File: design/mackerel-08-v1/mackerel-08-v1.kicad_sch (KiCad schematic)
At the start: 38 parts, among them J2 DC_Jack, J3 Conn_01x06, J4 Conn_01x06, J5 Conn_02x20_Odd_Even, SW1 SW_Push, U1 MC68008, U10 74HC595, U11 74HC10, U12 GAL16V8, U13 GAL16V8, U14 NE555P, U2 AS7C4096A, U3 AS7C4096A, U4 AS7C4096A, U5 AS7C4096A, U6 AS7C4096A, U7 AS7C4096A, U8 SST39SF040, U9 XR68C681, X1 CXO_DIP8, X2 CXO_DIP8

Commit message: Full interrupt and IACK decoding in PLD
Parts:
- removed J5: Conn_02x20_Odd_Even, Connector_PinHeader_2.54mm:PinHeader_2x20_P2.54mm_Vertical, symbol Connector_Generic:Conn_02x20_Odd_Even
- removed U12, U13: GAL16V8, Package_DIP:DIP-20_W7.62mm_Socket_LongPads, symbol Logic_Programmable:GAL16V8
- added U12, U?: ATF22V10C, Package_DIP:DIP-24_W7.62mm_Socket_LongPads, symbol mackerel-68k-symbols:ATF22V10C
- added U?: AS7C4096A, Package_SO:SOJ-36_10.16x23.49mm_P1.27mm, symbol mackerel-68k-symbols:AS7C4096A
- U14: footprint Package_DIP:DIP-8_W7.62mm -> Package_DIP:DIP-8_W7.62mm_Socket_LongPads
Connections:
- net +5V: now also U12.24 (vcc), U?.24 (vcc), U?.27 (VCC), U?.9 (VCC)
- net A0: now also U?.1 (A0)
- net A1: now also U12.4 (IN3/PD), U?.2 (A1), U?.9 (IN8)
- net A10: now also U?.20 (A10)
- net A11: now also U?.21 (A11)
- net A12: now also U?.22 (A12)
- net A13: now also U?.23 (A13)
- net A14: now also U?.24 (A14)
- net A15: now also U?.32 (A15)
- net A16: now also U12.7 (IN6), U?.33 (A16)
- net A17: now also U12.8 (IN7), U?.34 (A17)
- net A18: now also U12.9 (IN8), U?.35 (A18)
- net A19: now also U12.10 (IN9)
- net A2: now also U12.5 (IN4), U?.10 (IN9), U?.3 (A2)
- net A20: now also U12.11 (IN10)
- net A21: now also U12.13 (IN11)
- net A3: now also U12.6 (IN5), U?.11 (IN10), U?.4 (A3)
- net A4: now also U?.5 (A4)
- net A5: now also U?.14 (A5)
- net A6: now also U?.15 (A6)
- net A7: now also U?.16 (A7)
- net A8: now also U?.17 (A8)
- net A9: now also U?.18 (A9)
- net BOOT: now also U12.1 (CLK/IN0)
- net D0: now also U?.7 (IO1)
- net D1: now also U?.8 (IO2)
- net D2: now also U?.11 (IO3)
- net D3: now also U?.12 (IO4)
- net D4: now also U?.25 (IO5)
- net D5: now also U?.26 (IO6)
- net D6: now also U?.29 (IO7)
- net D7: now also U?.30 (IO8)
- net GND: now also U12.12 (GND), U?.10 (GND), U?.12 (GND), U?.28 (GND), U?.31 (OE)
- net RAM_EN0: now also U12.19 (IO5)
- net RAM_EN1: now also U12.18 (IO4)
- net RAM_EN2: now also U12.17 (IO3)
- net RAM_EN3: now also U12.16 (IO2)
- net RAM_EN4: now also U12.15 (IO1)
- net RAM_EN5: now also U12.14 (IO0)
- net /AS: now also U12.2 (IN1), U?.13 (IN11)
- net /CS_DUART: now also U12.22 (IO8); no longer U9.39 (CS)
- net /CS_ROM: now also U12.20 (IO6)
- net /IACK: now also U12.3 (IN2), U?.8 (IN7)
- net /IACK_DUART: now also U12.23 (IO9); no longer R2.1, U9.41 (/IACK)
- net /IPL0: now also U?.21 (IO7)
- net /IPL1: now also U?.22 (IO8)
- net /IPL2: now also U?.23 (IO9)
- net /RW: now also U?.13 (WE)
- net /IRQ_DUART renamed /IRQ1
- net /IRQ1: now also U?.1 (CLK/IN0)
- new net RAM_EN6: U?.6 (CE)
- new net /CS0: U9.39 (CS)
- new net /CS_IO: U12.21 (IO7)
- new net /IACK1: R2.1, U9.41 (/IACK), U?.14 (IO0)
- new net /IACK2: U?.15 (IO1)
- new net /IACK3: U?.16 (IO2)
- new net /IACK4: U?.17 (IO3)
- new net /IACK5: U?.18 (IO4)
- new net /IACK6: U?.19 (IO5)
- new net /IACK7: U?.20 (IO6)
- new net /IRQ2: U?.2 (IN1)
- new net /IRQ3: U?.3 (IN2)
- new net /IRQ4: U?.4 (IN3/PD)
- new net /IRQ5: U?.5 (IN4)
- new net /IRQ6: U?.6 (IN5)
- new net /IRQ7: U?.7 (IN6)
- no-connect marks 76 -> 38
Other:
- note added: "Interrupt/IACK Decoder"
- note removed: "Address/Interrupt Decoder"
- note removed: "RAM Chip Selector"
- note removed: "TODO: redo this bus layout"
- moved on the sheet: C1, D1, D2, R10, R11, R12, R13, SW1, U14, U6, U7

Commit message: Mackerel-08 mostly routed
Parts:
- removed J3, J4: Conn_01x06, Connector_PinHeader_2.54mm:PinHeader_1x06_P2.54mm_Vertical, symbol Connector_Generic:Conn_01x06
- removed R1: R, Resistor_SMD:R_1206_3216Metric_Pad1.30x1.75mm_HandSolder, symbol Device:R
- removed U11: 74HC10, Package_DIP:DIP-14_W7.62mm_Socket_LongPads, symbol mackerel-68k-symbols:74HC10
- removed U?: AS7C4096A, Package_SO:SOJ-36_10.16x23.49mm_P1.27mm, symbol mackerel-68k-symbols:AS7C4096A
- added J1: Conn_02x20_Odd_Even, Connector_PinSocket_2.54mm:PinSocket_2x20_P2.54mm_Horizontal, symbol Connector_Generic:Conn_02x20_Odd_Even
- added J3, J4: Conn_02x10_Odd_Even, Connector_PinSocket_2.54mm:PinSocket_2x10_P2.54mm_Horizontal, symbol Connector_Generic:Conn_02x10_Odd_Even
- added J5, J6: Conn_01x06, Connector_PinSocket_2.54mm:PinSocket_1x06_P2.54mm_Horizontal, symbol Connector_Generic:Conn_01x06
- added U13: 74HC10, Package_DIP:DIP-14_W7.62mm_Socket_LongPads, symbol mackerel-68k-symbols:74HC10
- added U8: AS7C4096A, Package_SO:SOJ-36_10.16x23.49mm_P1.27mm, symbol mackerel-68k-symbols:AS7C4096A
- U9: renamed from U8; footprint Package_DIP:DIP-32_W15.24mm_Socket_LongPads -> Socket:DIP_Socket-32_W11.9_W12.7_W15.24_W17.78_W18.5_3M_232-1285-00-0602J
- gave numbers to parts that had none: 1
- renumbered U9 to U10, U10 to U11, U14 to U15
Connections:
- net /CS0 is gone; now on net /DUART0: U10.39 (CS)
- net /CS_DUART is gone; now on net /RAM1: U12.22 (IO8)
- net /IACK_DUART is gone; now on net /RAM0: U12.23 (IO9)
- net +5V: now also J1.1 (Pin_1), J1.2 (Pin_2), J3.1 (Pin_1), J3.2 (Pin_2), J4.1 (Pin_1), J4.2 (Pin_2), U13.14 (VCC), U8.27 (VCC), U8.9 (VCC)
- net A0: now also J1.13 (Pin_13), U8.1 (A0)
- net A1: now also J1.14 (Pin_14), U8.2 (A1); no longer U12.4 (IN3/PD)
- net A10: now also J1.25 (Pin_25), U8.20 (A10)
- net A11: now also J1.26 (Pin_26), U8.21 (A11)
- net A12: now also J1.27 (Pin_27), U8.22 (A12)
- net A13: now also J1.28 (Pin_28), U8.23 (A13)
- net A14: now also J1.29 (Pin_29), U8.24 (A14)
- net A15: now also J1.30 (Pin_30), U8.32 (A15)
- net A16: now also J3.3 (Pin_3), U8.33 (A16)
- net A17: now also J3.4 (Pin_4), U8.34 (A17)
- net A18: now also J3.5 (Pin_5), U8.35 (A18)
- net A19: now also J3.6 (Pin_6)
- net A2: now also J1.15 (Pin_15), U8.3 (A2); no longer U12.5 (IN4)
- net A20: now also J3.7 (Pin_7)
- net A21: now also J3.8 (Pin_8)
- net A3: now also J1.16 (Pin_16), U8.4 (A3); no longer U12.6 (IN5)
- net A4: now also J1.17 (Pin_17), U8.5 (A4)
- net A5: now also J1.18 (Pin_18), U8.14 (A5)
- net A6: now also J1.19 (Pin_19), U8.15 (A6)
- net A7: now also J1.20 (Pin_20), U8.16 (A7)
- net A8: now also J1.23 (Pin_23), U8.17 (A8)
- net A9: now also J1.24 (Pin_24), U8.18 (A9)
- net D0: now also J1.5 (Pin_5), U8.7 (IO1)
- net D1: now also J1.6 (Pin_6), U8.8 (IO2)
- net D2: now also J1.7 (Pin_7), U8.11 (IO3)
- net D3: now also J1.8 (Pin_8), U8.12 (IO4)
- net D4: now also J1.9 (Pin_9), U8.25 (IO5)
- net D5: now also J1.10 (Pin_10), U8.26 (IO6)
- net D6: now also J1.11 (Pin_11), U8.29 (IO7)
- net D7: now also J1.12 (Pin_12), U8.30 (IO8)
- net GND: now also J1.21 (Pin_21), J1.22 (Pin_22), J1.3 (Pin_3), J1.39 (Pin_39), J1.4 (Pin_4), J1.40 (Pin_40), J3.19 (Pin_19), J3.20 (Pin_20), J4.18 (Pin_18), J4.20 (Pin_20), J4.3 (Pin_3), J4.4 (Pin_4), J5.6 (Pin_6), J6.6 (Pin_6), U13.1 (1A), U13.10 (3B), U13.11 (3C), U13.13 (1C), U13.2 (1B), U13.7 (GND), U13.9 (3A), U8.10 (GND), U8.28 (GND), U8.31 (OE)
- net /AS: now also J1.31 (Pin_31)
- net /CS_IO: now also U12.14 (IO0), J1.35 (Pin_35); no longer U12.21 (IO7)
- net /DS: now also J1.32 (Pin_32)
- net /DTACK: now also J1.33 (Pin_33)
- net /IACK: now also J1.34 (Pin_34), U13.6 (2Y)
- net /IACK2: now also J1.38 (Pin_38)
- net /IACK3: now also J3.10 (Pin_10)
- net /IACK4: now also J3.12 (Pin_12)
- net /IACK5: now also J3.14 (Pin_14)
- net /IACK6: now also J3.16 (Pin_16)
- net /IACK7: now also J3.18 (Pin_18)
- net /IRQ2: now also J1.37 (Pin_37)
- net /IRQ3: now also J3.9 (Pin_9)
- net /IRQ4: now also J3.11 (Pin_11)
- net /IRQ5: now also J3.13 (Pin_13)
- net /IRQ6: now also J3.15 (Pin_15)
- net /IRQ7: now also J3.17 (Pin_17)
- net /RESET: now also J1.36 (Pin_36)
- net /RW: now also U8.13 (WE)
- net at R7.1: now also U1.36 (/BGACK); no longer U1.37 (/BR)
- net OP1: now reaches U10.14 (OP1)
- net OP1: now also J4.7 (Pin_7)
- net OP3: now reaches U10.15 (OP3)
- net OP3: now also J4.11 (Pin_11)
- net OP5: now reaches U10.16 (OP5)
- net OP5: now also J4.15 (Pin_15)
- net OP7: now reaches U10.17 (OP7)
- net OP7: now also J4.19 (Pin_19)
- net OP6: now reaches U10.29 (OP6)
- net OP6: now also J4.17 (Pin_17)
- net IP3: now reaches U10.3 (IP3)
- net IP3: now also J4.12 (Pin_12)
- net OP4: now reaches U10.30 (OP4)
- net OP4: now also J4.13 (Pin_13)
- net OP2: now reaches U10.31 (OP2)
- net OP2: now also J4.9 (Pin_9)
- net OP0: now reaches U10.32 (OP0)
- net OP0: now also J4.5 (Pin_5)
- net IP2: now reaches U10.40 (IP2)
- net IP2: now also J4.10 (Pin_10)
- net IP5: now reaches U10.42 (IP5)
- net IP5: now also J4.16 (Pin_16)
- net IP4: now reaches U10.43 (IP4)
- net IP4: now also J4.14 (Pin_14)
- net IP1: now reaches U10.5 (IP1)
- net IP1: now also J4.8 (Pin_8)
- net IP0: now reaches U10.8 (IP0)
- net IP0: now also J4.6 (Pin_6)
- net at R6.1: now also U1.37 (/BR); no longer U1.43 (/VPA)
- net at R8.1: now also U1.44 (/BERR); no longer U1.36 (/BGACK)
- net CLK_CPU: now reaches U1.38 (CLK), X1.5 (OUT)
- net at R9.1: now also U1.43 (/VPA); no longer U1.44 (/BERR)
- net FC0: no longer names the net of U1.50 (FC0)
- net FC0: now also U13.5 (2C)
- net FC1: no longer names the net of U1.49 (FC1)
- net FC1: now also U13.4 (2B)
- net FC2: no longer names the net of U1.48 (FC2)
- net FC2: now also U13.3 (2A)
- net RAM_EN0 renamed /RAM0
- net /RAM0: no longer U12.19 (IO5)
- net RAM_EN1 renamed /RAM1
- net /RAM1: no longer U12.18 (IO4)
- net RAM_EN2 renamed /RAM2
- net /RAM2: now also U12.21 (IO7); no longer U12.17 (IO3)
- net RAM_EN3 renamed /RAM3
- net /RAM3: now also U12.20 (IO6); no longer U12.16 (IO2)
- net RAM_EN4 renamed /DUART0
- net /DUART0: no longer U6.6 (CE)
- net RAM_EN5 renamed /RAM5
- net /RAM5: now also U12.18 (IO4); no longer U12.14 (IO0)
- net RXA: no longer names the net of U10.35 (RXDA)
- net RXA: now also J5.3 (Pin_3)
- net RXB: no longer names the net of U10.11 (RXDB)
- net RXB: now also J6.3 (Pin_3)
- net TXA: no longer names the net of U10.33 (TXDA)
- net TXA: now also J5.2 (Pin_2)
- net TXB: no longer names the net of U10.13 (TXDB)
- net TXB: now also J6.2 (Pin_2)
- net /CS_ROM renamed /ROM0
- net /ROM0: now also U12.16 (IO2); no longer U12.20 (IO6)
- new net /RAM4: U12.19 (IO5), U6.6 (CE)
- new net /RAM6: U12.17 (IO3), U8.6 (CE)
- no-connect marks 38 -> 27
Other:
- note added: "TODO: Am I using autovector or normal vector?"
- note added: "TODO: Does DTACK factor into IACK signals?"
- note removed: "TODO: expose GPIO pins"
- moved on the sheet: C1, C2, D1, D2, J2, R10, R11, R12, R13, R2, R3, R4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

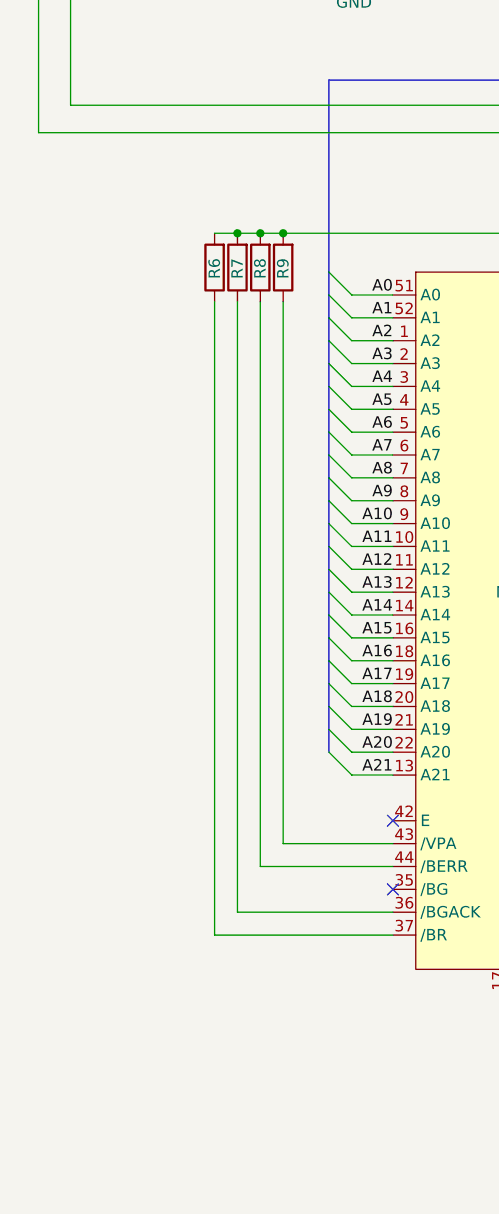
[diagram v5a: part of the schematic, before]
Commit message: Add decoupling caps
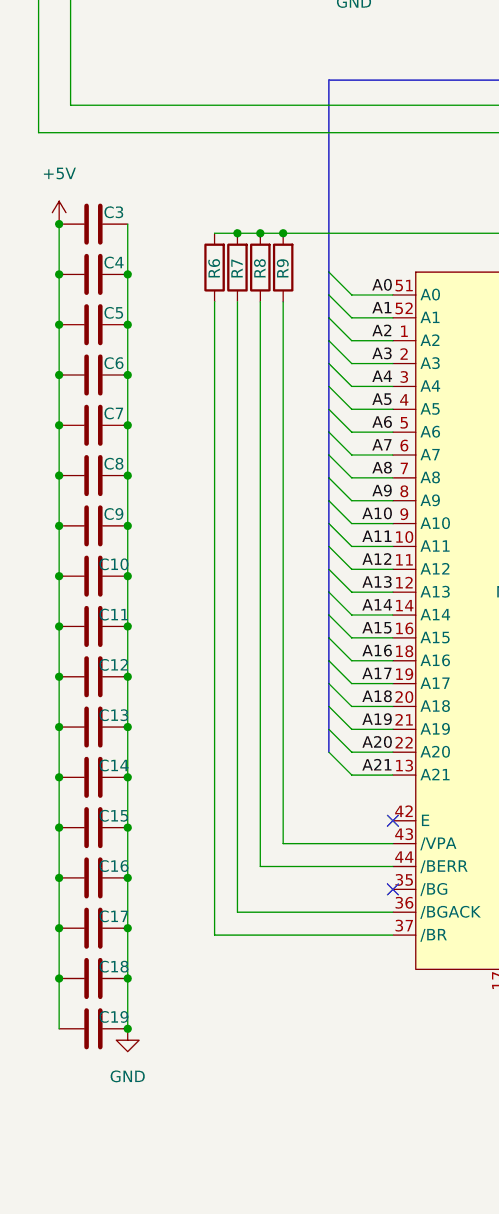
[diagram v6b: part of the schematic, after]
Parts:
- added C10, C11, C12, C13, C14, C15, C16, C17, C18, C19, C3, C4, C5, C6, C7, C8, C9: C, Capacitor_THT:C_Disc_D3.0mm_W2.0mm_P2.50mm, symbol Device:C
- R10, R11, R12, R13, R2, R3, R4, R5, R6, R7, R8, R9: footprint Resistor_SMD:R_1206_3216Metric_Pad1.30x1.75mm_HandSolder -> Resistor_THT:R_Axial_DIN0207_L6.3mm_D2.5mm_P7.62mm_Horizontal
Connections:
- net +5V: now also C10.1, C11.1, C12.1, C13.1, C14.1, C15.1, C16.1, C17.1, C18.1, C19.1, C3.1, C4.1, C5.1, C6.1, C7.1, C8.1, C9.1
- net GND: now also C10.2, C11.2, C12.2, C13.2, C14.2, C15.2, C16.2, C17.2, C18.2, C19.2, C3.2, C4.2, C5.2, C6.2, C7.2, C8.2, C9.2

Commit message: Rough layout of Mackerel-08 Rev1 PCB
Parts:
- removed J1: Conn_02x20_Odd_Even, Connector_PinSocket_2.54mm:PinSocket_2x20_P2.54mm_Horizontal, symbol Connector_Generic:Conn_02x20_Odd_Even
- removed J3, J4: Conn_02x10_Odd_Even, Connector_PinSocket_2.54mm:PinSocket_2x10_P2.54mm_Horizontal, symbol Connector_Generic:Conn_02x10_Odd_Even
- removed J5, J6: Conn_01x06, Connector_PinSocket_2.54mm:PinSocket_1x06_P2.54mm_Horizontal, symbol Connector_Generic:Conn_01x06
- removed U13: 74HC10, Package_DIP:DIP-14_W7.62mm_Socket_LongPads, symbol mackerel-68k-symbols:74HC10
- removed U2, U3, U4, U5, U6, U7, U8: AS7C4096A, Package_SO:SOJ-36_10.16x23.49mm_P1.27mm, symbol mackerel-68k-symbols:AS7C4096A
- added C20, C21, C22, C23, C24, C25, C26, C27: C_Polarized_US, Capacitor_THT:CP_Radial_Tantal_D4.5mm_P5.00mm, symbol Device:C_Polarized_US
- added D3: LED, LED_THT:LED_D5.0mm, symbol Device:LED
- added H1, H2, H3, H4: MountingHole, MountingHole:MountingHole_3.7mm_Pad_Via, symbol Mechanical:MountingHole
- added J1: Conn_01x08, Connector_PinSocket_2.54mm:PinSocket_1x08_P2.54mm_Vertical, symbol Connector_Generic:Conn_01x08
- added J3: Conn_02x20_Counter_Clockwise, symbol Connector_Generic:Conn_02x20_Counter_Clockwise
- added J4: Conn_02x20_Counter_Clockwise, Connector_IDC:IDC-Header_2x20_P2.54mm_Vertical, symbol Connector_Generic:Conn_02x20_Counter_Clockwise
- added J5, J6: DB9_Male_MountingHoles, Connector_Dsub:DSUB-9_Male_Horizontal_P2.77x2.84mm_EdgePinOffset7.70mm_Housed_MountingHolesOffset9.12mm, symbol Connector:DB9_Male_MountingHoles
- added R1, R14, R15: R, Resistor_THT:R_Axial_DIN0207_L6.3mm_D2.5mm_P7.62mm_Horizontal, symbol Device:R
- added SW2: SW_SPDT, herring:SW_Mini_Toggle, symbol Switch:SW_SPDT
- added U13, U16: MAX3232, Package_DIP:DIP-16_W7.62mm, symbol Interface_UART:MAX3232
- added U2, U3, U4, U5, U6, U7, U8: AS6C4008-55PCN, Package_DIP:DIP-32_W15.24mm, symbol Memory_RAM:AS6C4008-55PCN
- U11: footprint Package_DIP:DIP-16_W7.62mm_Socket_LongPads -> Package_DIP:DIP-16_W7.62mm
- U12, U14: footprint Package_DIP:DIP-24_W7.62mm_Socket_LongPads -> Package_DIP:DIP-24_W7.62mm
- U15: footprint Package_DIP:DIP-8_W7.62mm_Socket_LongPads -> Package_DIP:DIP-8_W7.62mm
- U9: footprint Socket:DIP_Socket-32_W11.9_W12.7_W15.24_W17.78_W18.5_3M_232-1285-00-0602J -> Package_DIP:DIP-32_W15.24mm
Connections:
- net /IACK6 is gone; now on net /IACK: U14.19 (IO5)
- net /IRQ4 is gone; now on net FC0: U14.4 (IN3/PD)
- net /IRQ5 is gone; now on net FC1: U14.5 (IN4)
- net /IRQ6 is gone; now on net FC2: U14.6 (IN5)
- net +5V: now also J1.1 (Pin_1), R14.2, R15.2, U13.16 (VCC), U16.16 (VCC), U2.32 (VCC), U3.32 (VCC), U4.32 (VCC), U5.32 (VCC), U6.32 (VCC), U7.32 (VCC), U8.32 (VCC)
- net A0: now also U2.12 (A0), U3.12 (A0), U4.12 (A0), U5.12 (A0), U6.12 (A0), U7.12 (A0), U8.12 (A0)
- net A1: now also U2.11 (A1), U3.11 (A1), U4.11 (A1), U5.11 (A1), U6.11 (A1), U7.11 (A1), U8.11 (A1)
- net A10: now also U2.23 (A10), U3.23 (A10), U4.23 (A10), U5.23 (A10), U6.23 (A10), U7.23 (A10), U8.23 (A10)
- net A11: now also U2.25 (A11), U3.25 (A11), U4.25 (A11), U5.25 (A11), U6.25 (A11), U7.25 (A11), U8.25 (A11)
- net A12: now also U2.4 (A12), U3.4 (A12), U4.4 (A12), U5.4 (A12), U6.4 (A12), U7.4 (A12), U8.4 (A12)
- net A13: now also U2.28 (A13), U3.28 (A13), U4.28 (A13), U5.28 (A13), U6.28 (A13), U7.28 (A13), U8.28 (A13)
- net A14: now also U2.3 (A14), U3.3 (A14), U4.3 (A14), U5.3 (A14), U6.3 (A14), U7.3 (A14), U8.3 (A14)
- net A15: now also U2.31 (A15), U3.31 (A15), U4.31 (A15), U5.31 (A15), U6.31 (A15), U7.31 (A15), U8.31 (A15)
- net A16: now also U2.2 (A16), U3.2 (A16), U4.2 (A16), U5.2 (A16), U6.2 (A16), U7.2 (A16), U8.2 (A16)
- net A17: now also U2.30 (A17), U3.30 (A17), U4.30 (A17), U5.30 (A17), U6.30 (A17), U7.30 (A17), U8.30 (A17)
- net A18: now also U2.1 (A18), U3.1 (A18), U4.1 (A18), U5.1 (A18), U6.1 (A18), U7.1 (A18), U8.1 (A18)
- net A2: now also U2.10 (A2), U3.10 (A2), U4.10 (A2), U5.10 (A2), U6.10 (A2), U7.10 (A2), U8.10 (A2)
- net A3: now also U2.9 (A3), U3.9 (A3), U4.9 (A3), U5.9 (A3), U6.9 (A3), U7.9 (A3), U8.9 (A3)
- net A4: now also U2.8 (A4), U3.8 (A4), U4.8 (A4), U5.8 (A4), U6.8 (A4), U7.8 (A4), U8.8 (A4)
- net A5: now also U2.7 (A5), U3.7 (A5), U4.7 (A5), U5.7 (A5), U6.7 (A5), U7.7 (A5), U8.7 (A5)
- net A6: now also U2.6 (A6), U3.6 (A6), U4.6 (A6), U5.6 (A6), U6.6 (A6), U7.6 (A6), U8.6 (A6)
- net A7: now also U2.5 (A7), U3.5 (A7), U4.5 (A7), U5.5 (A7), U6.5 (A7), U7.5 (A7), U8.5 (A7)
- net A8: now also U2.27 (A8), U3.27 (A8), U4.27 (A8), U5.27 (A8), U6.27 (A8), U7.27 (A8), U8.27 (A8)
- net A9: now also U2.26 (A9), U3.26 (A9), U4.26 (A9), U5.26 (A9), U6.26 (A9), U7.26 (A9), U8.26 (A9)
- net D0: now also U2.13 (DQ0), U3.13 (DQ0), U4.13 (DQ0), U5.13 (DQ0), U6.13 (DQ0), U7.13 (DQ0), U8.13 (DQ0)
- net D1: now also U2.14 (DQ1), U3.14 (DQ1), U4.14 (DQ1), U5.14 (DQ1), U6.14 (DQ1), U7.14 (DQ1), U8.14 (DQ1)
- net D2: now also U2.15 (DQ2), U3.15 (DQ2), U4.15 (DQ2), U5.15 (DQ2), U6.15 (DQ2), U7.15 (DQ2), U8.15 (DQ2)
- net D3: now also U2.17 (DQ3), U3.17 (DQ3), U4.17 (DQ3), U5.17 (DQ3), U6.17 (DQ3), U7.17 (DQ3), U8.17 (DQ3)
- net D4: now also U2.18 (DQ4), U3.18 (DQ4), U4.18 (DQ4), U5.18 (DQ4), U6.18 (DQ4), U7.18 (DQ4), U8.18 (DQ4)
- net D5: now also U2.19 (DQ5), U3.19 (DQ5), U4.19 (DQ5), U5.19 (DQ5), U6.19 (DQ5), U7.19 (DQ5), U8.19 (DQ5)
- net D6: now also U2.20 (DQ6), U3.20 (DQ6), U4.20 (DQ6), U5.20 (DQ6), U6.20 (DQ6), U7.20 (DQ6), U8.20 (DQ6)
- net D7: now also U2.21 (DQ7), U3.21 (DQ7), U4.21 (DQ7), U5.21 (DQ7), U6.21 (DQ7), U7.21 (DQ7), U8.21 (DQ7)
- net GND: now also C24.2, C25.1, C26.2, C27.1, D3.1 (K), J1.3 (Pin_3), J5.0 (PAD), J5.5, J6.0 (PAD), J6.5, U13.15 (GND), U16.15 (GND), U2.16 (VSS), U2.24 (OE#), U3.16 (VSS), U3.24 (OE#), U4.16 (VSS), U4.24 (OE#), U5.16 (VSS), U5.24 (OE#), U6.16 (VSS), U6.24 (OE#), U7.16 (VSS), U7.24 (OE#), U8.16 (VSS), U8.24 (OE#); no longer U9.16 (GND), U9.24 (/OE)
- net /DUART0: no longer U10.39 (CS)
- net /IACK: no longer U14.8 (IN7)
- net /IACK1: no longer R2.1, U10.41 (/IACK)
- net /IRQ1: no longer U10.24 (INTR)
- net /RAM0: now also U2.22 (CE#)
- net /RAM1: now also U3.22 (CE#)
- net /RAM2: now also U4.22 (CE#)
- net /RAM3: now also U5.22 (CE#)
- net /RAM4: now also U7.22 (CE#)
- net /RAM5: now also U6.22 (CE#)
- net /RAM6: now also U8.22 (CE#)
- net /RW: now also U2.29 (WE#), U3.29 (WE#), U4.29 (WE#), U5.29 (WE#), U6.29 (WE#), U7.29 (WE#), U8.29 (WE#)
- net RXB: now reaches U10.11 (RXDB)
- net TXB: now reaches U10.13 (TXDB)
- net TXA: now reaches U10.33 (TXDA)
- net TXA: now also U13.11 (T1IN)
- net RXA: now reaches U10.35 (RXDA)
- net RXA: now also U13.12 (R1OUT)
- net FC2: now reaches U1.48 (FC2)
- net FC1: now reaches U1.49 (FC1)
- net FC0: now reaches U1.50 (FC0)
- net CLK_DUART: no longer names the net of U10.36 (X1/CLK), X2.5 (OUT)
- net IP0 renamed /CTSA
- net /CTSA: now also U13.9 (R2OUT)
- net IP1 renamed /CTSB
- net IP2 renamed SD_CD
- net SD_CD: now also J1.8 (Pin_8)
- net IP3 renamed SPI_DO
- net SPI_DO: now also J1.5 (Pin_5)
- net IP4: no longer names the net of U10.43 (IP4)
- net IP4: now also R14.1
- net IP5: no longer names the net of U10.42 (IP5)
- net IP5: now also R15.1
- net OP0 renamed /RTSA
- net /RTSA: now also U13.10 (T2IN)
- net OP1 renamed /RTSB
- net OP2 renamed SPI_DI
- net SPI_DI: now also J1.6 (Pin_6)
- net OP3 renamed SPI_CLK
- net SPI_CLK: now also J1.4 (Pin_4)
- net OP4 renamed SPI_CS0
- net SPI_CS0: now also J1.7 (Pin_7)
- net OP5 renamed SPI_CS1
- net OP6 renamed SPI_CS2
- net OP7 renamed LED_U0
- net LED_U0: now also R1.1
- net /DTACK renamed /DTACK_CPU
- net /IACK3: no longer names the net of U14.16 (IO2)
- net /IACK4: no longer names the net of U14.17 (IO3)
- net /IACK5: no longer names the net of U14.18 (IO4)
- net /IACK7: no longer names the net of U14.20 (IO6)
- net /IRQ3: no longer names the net of U14.3 (IN2)
- net /IRQ7: no longer names the net of U14.7 (IN6)
- new net: C22.1, U13.4 (C2+)
- new net: C22.2, U13.5 (C2-)
- new net: C20.1, U13.1 (C1+)
- new net: C20.2, U13.3 (C1-)
- new net: D3.2 (A), R1.2
- new net: C23.1, U16.4 (C2+)
- new net: C23.2, U16.5 (C2-)
- new net: J6.2, U16.13 (R1IN)
- new net: J6.3, U16.14 (T1OUT)
- new net: J6.7, U16.7 (T2OUT)
- new net: J6.8, U16.8 (R2IN)
- new net: C24.1, U13.2 (VS+)
- new net: C25.2, U13.6 (VS-)
- new net: J5.2, U13.13 (R1IN)
- new net: J5.3, U13.14 (T1OUT)
- new net: J5.7, U13.7 (T2OUT)
- new net: J5.8, U13.8 (R2IN)
- new net: C27.2, U16.6 (VS-)
- new net: U9.16 (GND), U9.24 (/OE)
- new net: C26.1, U16.2 (VS+)
- new net: C21.1, U16.1 (C1+)
- new net: C21.2, U16.3 (C1-)
- new net /DUART: U10.39 (CS)
- new net /IACK_DUART: R2.1, U10.41 (/IACK)
- new net /INT_DUART: U10.24 (INTR)
- no-connect marks 27 -> 25
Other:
- note added: "IACK factors into DTACK"
- note added: "MC68008 CPU"
- note added: "Power-on Reset"
- note added: "TODO: check the pinout of CTS/RTS and the DB-9 connector"
- note added: "TODO: do something with DTACK"
- note added: "TODO: power switch"
- note removed: "Interrupt/IACK Decoder"
- note removed: "TODO: Am I using autovector or normal vector?"
- note removed: "TODO: Does DTACK factor into IACK signals?"
- note removed: "TODO: is AS the correct pin here?"
- moved on the sheet: C1, C10, C11, C12, C13, C14, C15, C16, C17, C18, C19, C2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
